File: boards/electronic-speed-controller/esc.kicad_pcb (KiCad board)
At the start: 4 copper layers, 64.8 x 84.5 mm, 83 parts, among them J101 XT60PW-M, J102 39303037, K101 G5PZ-1A4-E, SW101 1825255-1, U101 LMR51420XDDCR, U102 Teensy4.1, U201 MIC4605-2YM-TR, U202 SISHA14DN-T1-GE3, U203 SISHA14DN-T1-GE3, U204 INA180A3IDBVR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

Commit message: updated MOSFETs
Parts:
- removed K101: G5PZ-1A4-E, G5PZ-1A4-E:G5PZ_OMR
- removed SW101: 1825255-1, SLIDE_SWITCH:SW3_1825255-1_TEC
- removed U202, U203, U302, U303, U402, U403: SISHA14DN-T1-GE3, N_MOSFETS:MOSFET_3DN-T1-GE3_VIS
- added D106: LED, LED_SMD:LED_0201_0603Metric, F.Cu at (22.5, 85.4)
- added D107: LED, LED_SMD:LED_0201_0603Metric, F.Cu at (22.5, 87.2)
- added Q201: BSC340N08NS3G, Package_TO_SOT_SMD:TDSON-8-1, F.Cu at (47.2, 92.6)
- added Q202: BSC340N08NS3G, Package_TO_SOT_SMD:TDSON-8-1, F.Cu at (50.4, 100.6)
- added Q301: BSC340N08NS3G, Package_TO_SOT_SMD:TDSON-8-1, F.Cu at (-9.39, 62.2)
- added Q302: BSC340N08NS3G, Package_TO_SOT_SMD:TDSON-8-1, F.Cu at (-9.39, 68.9)
- added Q401: BSC340N08NS3G, Package_TO_SOT_SMD:TDSON-8-1, F.Cu at (-9.39, 77.6)
- added Q402: BSC340N08NS3G, Package_TO_SOT_SMD:TDSON-8-1, F.Cu at (-9.39, 84.3)
- added R111: 100, Resistor_SMD:R_0603_1608Metric, F.Cu at (21.2, 77.6)
- added R112: 100, Resistor_SMD:R_0603_1608Metric, F.Cu at (21.2, 80.1)
- added R113: 10k, Resistor_SMD:R_0603_1608Metric, F.Cu at (2.73, 75.5)
- added R114: 10k, Resistor_SMD:R_0603_1608Metric, F.Cu at (2.73, 78.0)
- added R115: 10k, Resistor_SMD:R_0603_1608Metric, F.Cu at (2.73, 80.5)
- added R401: 100, Resistor_SMD:R_0603_1608Metric, F.Cu at (-3.28, 75.5)
- added R402: 100, Resistor_SMD:R_0603_1608Metric, F.Cu at (-3.28, 78.0)
- D105: footprint LED_SMD:LED_2512_6332Metric -> LED_SMD:LED_0201_0603Metric
- F101: value 20A -> 15A
- R301, R302: moved to F.Cu
- moved R301 60.4 mm to (-3.28, 60.1), turned to 0 degrees
- moved R302 58.0 mm to (-3.28, 62.6), turned to 0 degrees
- moved R402 54.5 mm to (53.3, 66.5), turned to 180 degrees
- moved R403 29.5 mm to (35.2, 63.0), turned to 180 degrees
- moved C403 21.8 mm to (21.3, 57.9)
- moved C404 21.8 mm to (21.3, 62.2)
- moved C406 21.8 mm to (16.5, 54.7)
- moved R405 21.8 mm to (16.5, 67.2)
- moved C402 21.8 mm to (20.7, 68.8)
- moved C405 21.8 mm to (16.5, 52.1)
- moved R401 21.8 mm to (16.5, 59.7)
- moved C407 21.8 mm to (16.5, 57.2)
- moved D401 21.8 mm to (24.6, 65.1)
- moved R404 21.8 mm to (16.5, 64.7)
- moved R406 21.8 mm to (16.5, 69.7)
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- renumbered R108 to R105, R109 to R106, R105 to R107, R106 to R108, R107 to R109
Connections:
- C203 pad 1: V_MOT -> VCC
- C204 pad 1: V_MOT -> VCC
- C303 pad 1: V_MOT -> VCC
- C304 pad 1: V_MOT -> VCC
- C403 pad 1: V_MOT -> VCC
- C404 pad 1: V_MOT -> VCC
- R110 pad 1: V_MOT -> I_ERROR_A
- R203 pad 1: Net-(U204-IN+) -> Net-(U202-IN+)
- R204 pad 1: Net-(U204-OUT) -> Net-(U202-OUT)
- R303 pad 1: Net-(U304-IN+) -> Net-(U302-IN+)
- R304 pad 1: Net-(U304-OUT) -> Net-(U302-OUT)
- R403 pad 1: Net-(U404-IN+) -> Net-(U402-IN+)
- R404 pad 1: Net-(U404-OUT) -> Net-(U402-OUT)
- U102 pad 2: unconnected-(U102-0_RX1_CRX2_CS1-Pad2) -> I_ERROR_A
- U102 pad 3: unconnected-(U102-1_TX1_CTX2_MISO1-Pad3) -> I_ERROR_B
- U102 pad 4: unconnected-(U102-2_OUT2-Pad4) -> I_ERROR_C
- U102 pad 45: unconnected-(U102-23_A9_CRX1_MCLK1-Pad45) -> V_NEUTRAL
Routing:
- net Net-(K101-Pad1): track 40.9 -> 0.00 mm
- net VCC: track 35.7 -> 7.26 mm, vias 16 -> 17
- net V_SENSE_B: track 21.1 -> 0.00 mm, vias 2 -> 0
- net PHASE_A: track 15.8 -> 0.02 mm, vias 2 -> 0
- net GND: track 45.0 -> 30.9 mm, vias 41 -> 39
- net Net-(U301-LO): track 10.7 -> 0.00 mm
- net I_SENSE_B: track 10.8 -> 0.41 mm
- net Net-(U301-HO): track 8.41 -> 0.00 mm
- net PWM_B: track 7.81 -> 0.00 mm
- net Net-(Q301-G): track 4.50 -> 0.00 mm
- net Net-(Q202-G): track 4.23 -> 0.00 mm
- net Net-(Q302-G): track 3.97 -> 0.00 mm
- net PHASE_B: track 3.82 -> 0.00 mm
- net Net-(Q201-G): track 3.29 -> 0.00 mm
- net Net-(U304-OUT): track 2.04 -> 0.00 mm
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- added copper zone on F.Cu, net Net-(U202-IN+)
- removed copper zone on B.Cu, net +5V
- removed copper zone on F.Cu, net Net-(U204-IN+)
- removed copper zone on B.Cu, net Net-(U304-IN+)
- removed copper zone on F.Cu, net PHASE_A
- removed copper zone on B.Cu, net PHASE_B
- removed copper zone on B.Cu, net V_MOT
- removed copper zone on F.Cu, net V_MOT
- removed copper zone on In1.Cu, net V_MOT
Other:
- board text removed: "OFF"
- board text removed: "ON"

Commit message: finished layout and schematic
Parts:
- removed F101: 15A, Fuse:Fuse_1206_3216Metric
- removed the R401 at (16.5, 59.7)
- removed the R402 at (53.3, 66.5)
- added C107: 0.1uF, Capacitor_SMD:C_0603_1608Metric, F.Cu at (42.7, 91.9)
- added C108: 0.1uF, Capacitor_SMD:C_0603_1608Metric, F.Cu at (46.7, 91.9)
- added C109: 0.1uF, Capacitor_SMD:C_0603_1608Metric, F.Cu at (50.8, 91.9)
- added R116: 100, Resistor_SMD:R_0603_1608Metric, F.Cu at (44.4, 91.9)
- added R117: 100, Resistor_SMD:R_0603_1608Metric, F.Cu at (48.5, 91.9)
- added R118: 100, Resistor_SMD:R_0603_1608Metric, F.Cu at (52.6, 91.9)
- added U103: Teensy4.0, teensy.pretty-master:Teensy40, F.Cu at (96.9, 100.3)
- added U104: TL331, Package_TO_SOT_SMD:SOT-23-5, F.Cu at (47.6, 95.7)
- added U105: TL331, Package_TO_SOT_SMD:SOT-23-5, F.Cu at (51.7, 95.7)
- C201, C205, C401, C405, Q202, Q302, Q402, R110, R111, R112, R113, R114, R115, R202, R203, R302, R402, R403: moved to B.Cu
- C302, C303, C304, C306, C307, D301, R304, R305, R306, U301: moved to F.Cu
- U102: value Teensy4.1 -> TL331; footprint teensy.pretty-master:Teensy41 -> Package_TO_SOT_SMD:SOT-23-5
- U202: renamed from U204; moved to B.Cu
- U402: renamed from U404; moved to B.Cu
- moved Q301 85.5 mm to (63.8, 106.4)
- moved R302 85.1 mm to (66.7, 111.1), turned to 90 degrees
- moved R301 83.5 mm to (62.9, 111.1), turned to 90 degrees
- moved Q302 81.5 mm to (63.0, 106.4), turned to 180 degrees
- moved Q401 74.5 mm to (63.8, 91.9)
- moved Q402 72.5 mm to (62.7, 91.9), turned to 180 degrees
- moved R402 72.3 mm to (66.6, 96.6), turned to 90 degrees
- moved C405 71.4 mm to (73.4, 95.3), turned to -90 degrees
- moved C406 70.9 mm to (73.1, 97.3), turned to 180 degrees
- moved R401 69.3 mm to (62.8, 96.6), turned to 90 degrees
- moved C402 68.7 mm to (83.0, 97.9)
- moved C401 66.5 mm to (81.5, 92.8), turned to 90 degrees
- moved C407 62.2 mm to (64.7, 96.6), turned to -90 degrees
- moved R404 61.9 mm to (69.2, 97.3)
- moved R113 58.9 mm to (51.7, 108.2), turned to 180 degrees
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- renumbered U304 to U302
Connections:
- J101 pad 1: +BATT -> VCC
- U102 pad 1: GND -> V_NEUTRAL
- U102 pad 2: I_ERROR_A -> GND
- U102 pad 3: I_ERROR_B -> PHASE_A
- U102 pad 4: I_ERROR_C -> ZERO_A
- U102 pad 5: unconnected-(U102-3_LRCLK2-Pad5) -> VCC
- U202 pad 1: Net-(U204-OUT) -> Net-(U202-OUT)
- U202 pad 3: Net-(U204-IN+) -> Net-(U202-IN+)
- U302 pad 1: Net-(U304-OUT) -> Net-(U302-OUT)
- U302 pad 3: Net-(U304-IN+) -> Net-(U302-IN+)
- U402 pad 1: Net-(U404-OUT) -> Net-(U402-OUT)
- U402 pad 3: Net-(U404-IN+) -> Net-(U402-IN+)
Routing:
- net I_ERROR_C: track 0.00 -> 81.3 mm
- net I_ERROR_B: track 0.00 -> 76.1 mm
- net GND: track 30.9 -> 100.3 mm, vias 39 -> 31
- net I_ERROR_A: track 1.51 -> 70.4 mm, vias 1 -> 0
- net ZERO_A: track 0.00 -> 67.1 mm, vias 0 -> 1
- net ZERO_C: track 0.00 -> 66.3 mm, vias 0 -> 2
- net ZERO_B: track 0.00 -> 65.1 mm, vias 0 -> 2
- net +5V: track 33.3 -> 96.4 mm, vias 5 -> 7
- net V_SENSE_A: track 3.71 -> 59.4 mm, vias 0 -> 3
- net V_SENSE_B: track 0.00 -> 42.2 mm, vias 0 -> 2
- net V_SENSE_C: track 0.00 -> 41.9 mm, vias 0 -> 2
- net I_SENSE_A: track 8.34 -> 45.8 mm, vias 0 -> 1
- net PHASE_A: track 0.02 -> 37.2 mm
- net +3.3V: track 67.2 -> 102.1 mm, vias 0 -> 1
- net I_SENSE_B: track 0.41 -> 34.2 mm, vias 0 -> 1
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- added copper zone on B.Cu, net Net-(U202-IN+)
- added copper zone on B.Cu, net Net-(U302-IN+)
- added copper zone on B.Cu, net Net-(U402-IN+)
- added copper zone on B.Cu, net PHASE_A
- added copper zone on F.Cu, net PHASE_A
- added copper zone on B.Cu, net PHASE_B
- added copper zone on F.Cu, net PHASE_B
- added copper zone on B.Cu, net PHASE_C
- added copper zone on F.Cu, net PHASE_C
- removed copper zone on F.Cu, net +BATT
- removed copper zone on In1.Cu, net +BATT
- removed copper zone on F.Cu, net Net-(U202-IN+)
- removed copper zone on B.Cu, net VCC
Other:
- board size 64.8 x 84.5 mm -> 65.7 x 69.7 mm
- board text added: "ESC TESTING BOARD V1.0"
- board text added: "KH 12/30/23"
- board text added: "MOTOR ERR"
- board text added: "PHASE A"
- board text added: "PHASE B"
- board text added: "PHASE C"
- board text removed: "+MOTOR"

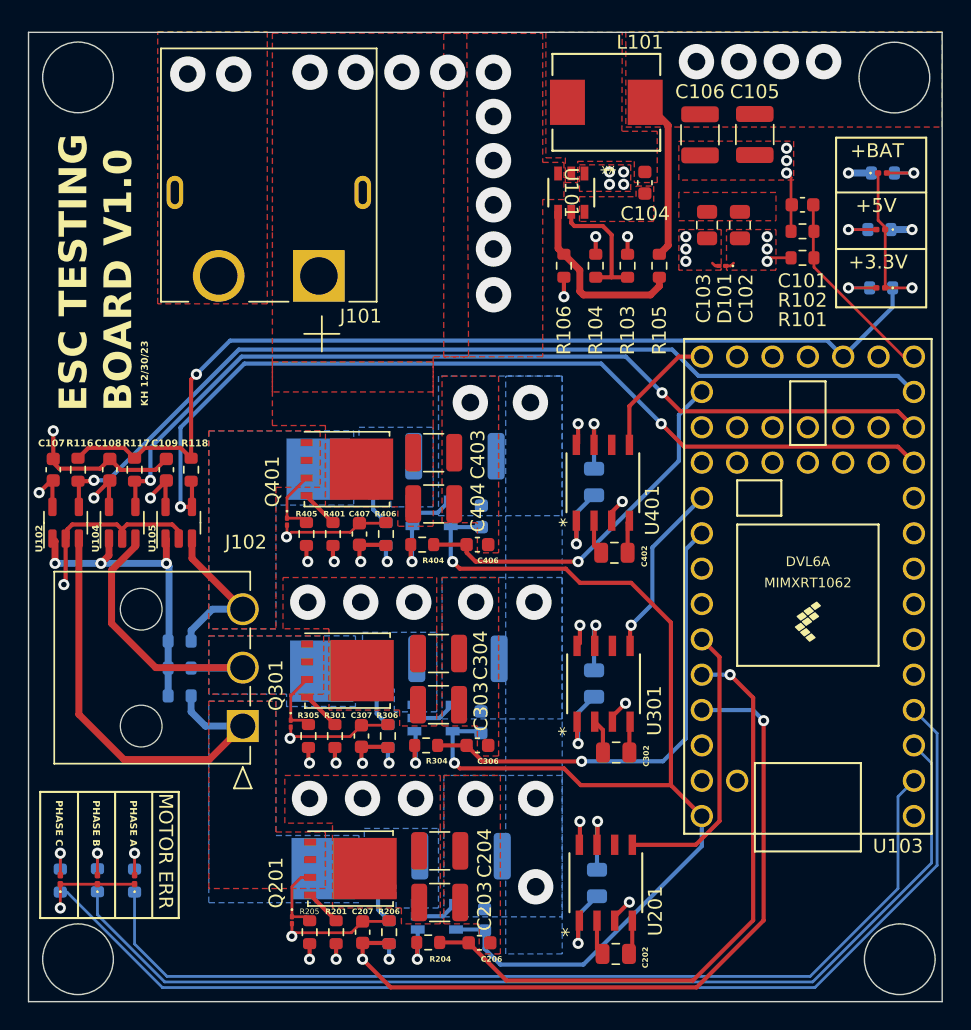
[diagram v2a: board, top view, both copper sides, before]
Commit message: simplified PHASE A circuit
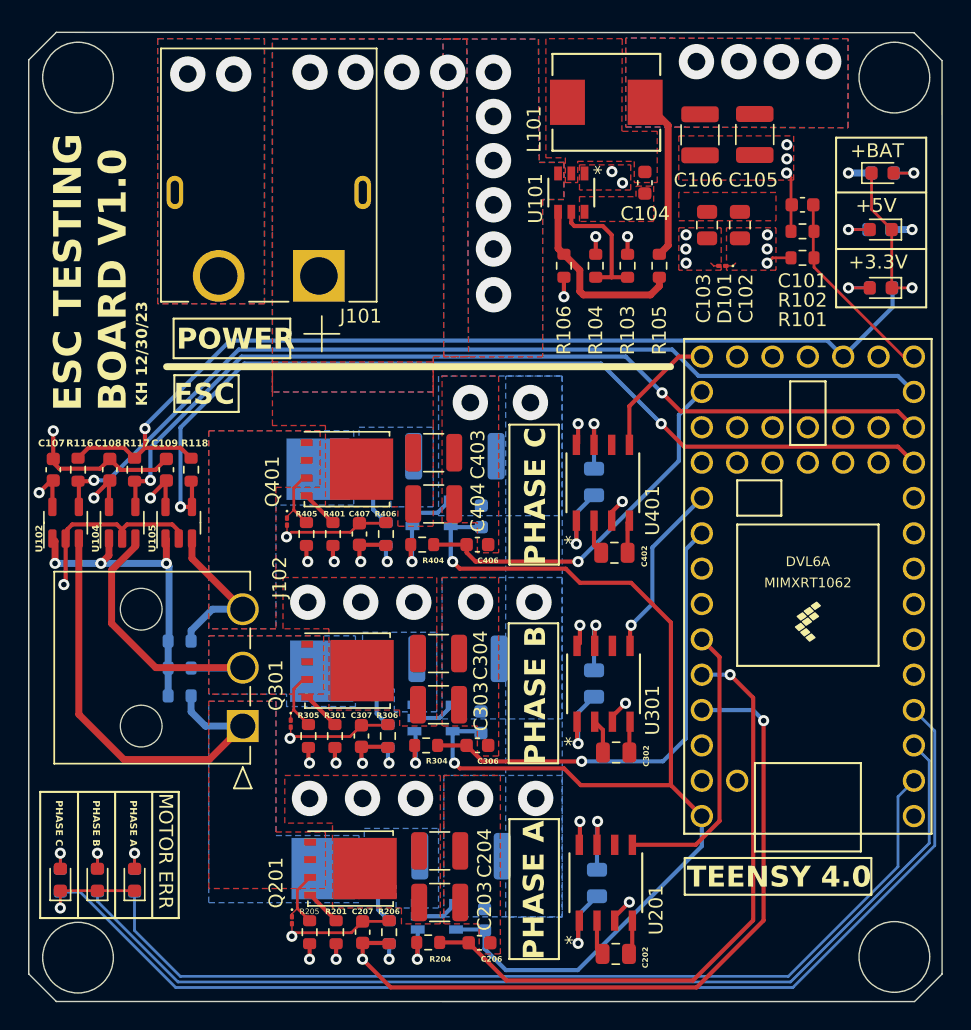
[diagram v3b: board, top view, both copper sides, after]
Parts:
- D102, D103, D104, D105, D106, D107: footprint LED_SMD:LED_0201_0603Metric -> LED_SMD:LED_0603_1608Metric
- R116, R117, R118: value 100 -> 4.7k
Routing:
- net I_ERROR_B: track 76.1 -> 74.5 mm
- net I_ERROR_A: track 70.4 -> 68.9 mm
- net I_ERROR_C: track 81.3 -> 80.3 mm
- net +3.3V: track 102.1 -> 102.9 mm
- net Net-(D103-A): track 3.47 -> 2.93 mm
- net PHASE_A: track 37.2 -> 36.7 mm
- net GND: track 100.3 -> 99.8 mm, vias 31 -> 28
- added copper zone on B.Cu, net +5V
- added copper zone on B.Cu, net VCC
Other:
- board size 65.7 x 69.7 mm -> 65.6 x 69.7 mm
- board text added: "ESC"
- board text added: "POWER"
- board text added: "TEENSY 4.0"
